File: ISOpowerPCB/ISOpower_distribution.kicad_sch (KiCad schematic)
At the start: 29 parts, among them M1 Fan_IEC60617, Q2 IRF5305_PBF, Q3 IRF5305_PBF, U10 LM2596S-5, U4 i6A4W020A-DC-DC-250W, U5 i6A4W020A-DC-DC-250W, U6 ACS712xLCTR-30A, U7 ACS712xLCTR-30A

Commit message: Started Routing V1
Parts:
- removed Q2, Q3: IRF5305_PBF, Package_TO_SOT_SMD:TO-263-2, symbol 000_MOSFET_Immo:IRF5305_PBF
- added Q2, Q3: Si2319CDS, Package_TO_SOT_SMD:SOT-23, symbol Transistor_FET:Si2319CDS
- R6, R7: footprint Resistor_THT:R_Axial_DIN0309_L9.0mm_D3.2mm_P12.70mm_Horizontal -> Resistor_THT:R_Axial_DIN0207_L6.3mm_D2.5mm_P7.62mm_Horizontal
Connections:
- net 12V_I_SENSE_OP is gone; now on net +12V: N2.1 (A), U7.3 (IP-), U7.4 (IP-)
- net 5V_I_SENSE_OP is gone; now on net +5V: N1.1 (A), U6.3 (IP-), U6.4 (IP-)
- net BUS_A_DISABLE: now also Q3.1 (G)
- net BUS_B_DISABLE: now also Q2.1 (G)
- net GND: now also Q2.3 (D), Q3.3 (D)
- net at JP2.2 (B), U4.2 (On/Off): now also Q2.2 (S)
- net at JP3.2 (B), U5.2 (On/Off): now also Q3.2 (S)
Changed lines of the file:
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@@
   (junction (at 246.38 133.35) (diameter 0) (color 0 0 0 0)
   )
+  (junction (at 173.99 64.77) (diameter 0) (color 0 0 0 0)
+  )
   (junction (at 205.74 128.27) (diameter 0) (color 0 0 0 0)
   )
@@
   (junction (at 246.38 143.51) (diameter 0) (color 0 0 0 0)
   )
+  (junction (at 179.07 64.77) (diameter 0) (color 0 0 0 0)
+  )
   (junction (at 39.37 39.37) (diameter 0) (color 0 0 0 0)
   )
@@
   (junction (at 113.03 64.77) (diameter 0) (color 0 0 0 0)
   )
+  (junction (at 170.18 143.51) (diameter 0) (color 0 0 0 0)
+  )
   (junction (at 121.92 143.51) (diameter 0) (color 0 0 0 0)
   )
@@
   )
   (junction (at 53.34 87.63) (diameter 0) (color 0 0 0 0)
+  )
+  (junction (at 175.26 143.51) (diameter 0) (color 0 0 0 0)
   )
   (junction (at 229.87 143.51) (diameter 0) (color 0 0 0 0)
@@
     (stroke (width 0) (type default) (color 0 0 0 0))
   )
-  (wire (pts (xy 149.86 143.51) (xy 171.45 143.51))
+  (wire (pts (xy 149.86 143.51) (xy 170.18 143.51))
     (stroke (width 0) (type default) (color 0 0 0 0))
   )
@@
     (stroke (width 0) (type default) (color 0 0 0 0))
   )
-  (wire (pts (xy 153.67 64.77) (xy 175.26 64.77))
+  (wire (pts (xy 153.67 64.77) (xy 173.99 64.77))
     (stroke (width 0) (type default) (color 0 0 0 0))
   )
@@
     (stroke (width 0) (type default) (color 0 0 0 0))
   )
-  (wire (pts (xy 176.53 143.51) (xy 173.99 143.51))
+  (wire (pts (xy 176.53 143.51) (xy 175.26 143.51))
     (stroke (width 0) (type default) (color 0 0 0 0))
   )
@@
     (stroke (width 0) (type default) (color 0 0 0 0))
   )
+  (wire (pts (xy 170.18 143.51) (xy 171.45 143.51))
+    (stroke (width 0) (type default) (color 0 0 0 0))
+  )
   (wire (pts (xy 59.69 153.67) (xy 59.69 154.94))
     (stroke (width 0) (type default) (color 0 0 0 0))
@@
     (stroke (width 0) (type default) (color 0 0 0 0))
   )
+  (wire (pts (xy 173.99 64.77) (xy 173.99 63.5))
+    (stroke (width 0) (type default) (color 0 0 0 0))
+  )
   (polyline (pts (xy 64.77 181.61) (xy 86.36 181.61))
     (stroke (width 0) (type default) (color 0 0 0 0))
   )
+  (wire (pts (xy 170.18 143.51) (xy 170.18 142.24))
+    (stroke (width 0) (type default) (color 0 0 0 0))
+  )
   (wire (pts (xy 246.38 143.51) (xy 246.38 142.24))
     (stroke (width 0) (type default) (color 0 0 0 0))
@@
     (stroke (width 0) (type default) (color 0 0 0 0))
   )
+  (wire (pts (xy 175.26 142.24) (xy 175.26 143.51))
+    (stroke (width 0) (type default) (color 0 0 0 0))
+  )
   (wire (pts (xy 246.38 134.62) (xy 246.38 133.35))
     (stroke (width 0) (type default) (color 0 0 0 0))
@@
     (stroke (width 0) (type default) (color 0 0 0 0))
   )
+  (wire (pts (xy 173.99 63.5) (xy 179.07 63.5))
+    (stroke (width 0) (type default) (color 0 0 0 0))
+  )
   (wire (pts (xy 41.91 80.01) (xy 41.91 81.28))
     (stroke (width 0) (type default) (color 0 0 0 0))
@@
     (stroke (width 0) (type default) (color 0 0 0 0))
   )
+  (wire (pts (xy 179.07 63.5) (xy 179.07 64.77))
+    (stroke (width 0) (type default) (color 0 0 0 0))
+  )
   (wire (pts (xy 143.51 64.77) (xy 143.51 62.23))
     (stroke (width 0) (type default) (color 0 0 0 0))
@@
     (stroke (width 0) (type default) (color 0 0 0 0))
   )
+  (wire (pts (xy 170.18 142.24) (xy 175.26 142.24))
+    (stroke (width 0) (type default) (color 0 0 0 0))
+  )
   (wire (pts (xy 41.91 146.05) (xy 41.91 143.51))
     (stroke (width 0) (type default) (color 0 0 0 0))
@@
     (stroke (width 0) (type default) (color 0 0 0 0))
   )
+  (wire (pts (xy 173.99 64.77) (xy 175.26 64.77))
+    (stroke (width 0) (type default) (color 0 0 0 0))
+  )
+  (wire (pts (xy 175.26 143.51) (xy 173.99 143.51))
+    (stroke (width 0) (type default) (color 0 0 0 0))
+  )
   (wire (pts (xy 217.17 133.35) (xy 214.63 133.35))
     (stroke (width 0) (type default) (color 0 0 0 0))
@@
     (stroke (width 0) (type default) (color 0 0 0 0))
   )
+  (wire (pts (xy 179.07 64.77) (xy 177.8 64.77))
+    (stroke (width 0) (type default) (color 0 0 0 0))
+  )
   (wire (pts (xy 158.75 125.73) (xy 158.75 130.81))
     (stroke (width 0) (type default) (color 0 0 0 0))
@@
     (stroke (width 0) (type default) (color 0 0 0 0))
   )
-  (wire (pts (xy 180.34 64.77) (xy 177.8 64.77))
+  (wire (pts (xy 180.34 64.77) (xy 179.07 64.77))
     (stroke (width 0) (type default) (color 0 0 0 0))
   )
@@
     (pin "2")
   )
+  (symbol (lib_id "Transistor_FET:Si2319CDS") (at 57.15 160.02 0) (mirror x) (unit 1)
+    (in_bom yes) (on_board yes)
+    (property "Reference" "Q2" (id 0) (at 60.96 154.94 90)
+      (effects (font (size 1.27 1.27)) (justify left))
+    )
+    (property "Value" "Si2319CDS" (id 1) (at 63.5 154.94 90)
+      (effects (font (size 1.27 1.27)) (justify left))
+    )
+    (property "Footprint" "Package_TO_SOT_SMD:SOT-23" (id 2) (at 62.23 158.115 0)
+      (effects (font (size 1.27 1.27) italic) (justify left) hide)
+    )
+    (property "Datasheet" "http://www.vishay.com/docs/66709/si2319cd.pdf" (id 3) (at 57.15 160.02 0)
+      (effects (font (size 1.27 1.27)) (justify left) hide)
+    )
+    (pin "1")
+    (pin "2")
+    (pin "3")
+  )
   (symbol (lib_id "000_Capacitor_Electrolytic_Immo:100u") (at 259.08 138.43 0) (unit 1)
     (in_bom yes) (on_board yes)
@@
       (effects (font (size 1.27 1.27)) (justify left))
     )
-    (property "Footprint" "Resistor_THT:R_Axial_DIN0309_L9.0mm_D3.2mm_P12.70mm_Horizontal" (id 2) (at 93.472 82.55 90)
+    (property "Footprint" "Resistor_THT:R_Axial_DIN0207_L6.3mm_D2.5mm_P7.62mm_Horizontal" (id 2) (at 93.472 82.55 90)
       (effects (font (size 1.27 1.27)) hide)
     )
@@
     (pin "1")
   )
-  (symbol (lib_id "000_MOSFET_Immo:IRF5305_PBF") (at 59.69 81.28 0) (mirror x) (unit 1)
-    (in_bom yes) (on_board yes)
-    (property "Reference" "Q3" (id 0) (at 57.15 83.82 90))
-    (property "Value" "IRF5305_PBF" (id 1) (at 66.04 81.28 90))
-    (property "Footprint" "Package_TO_SOT_SMD:TO-263-2" (id 2) (at 78.74 91.44 0)
+  (symbol (lib_id "Transistor_FET:Si2319CDS") (at 59.69 81.28 0) (mirror x) (unit 1)
+    (in_bom yes) (on_board yes)
+    (property "Reference" "Q3" (id 0) (at 63.5 76.2 90)
+      (effects (font (size 1.27 1.27)) (justify left))
+    )
+    (property "Value" "Si2319CDS" (id 1) (at 66.04 76.2 90)
+      (effects (font (size 1.27 1.27)) (justify left))
+    )
+    (property "Footprint" "Package_TO_SOT_SMD:SOT-23" (id 2) (at 64.77 79.375 0)
       (effects (font (size 1.27 1.27) italic) (justify left) hide)
     )
-    (property "Datasheet" "http://www.infineon.com/dgdl/irf4905.pdf?fileId=5546d462533600a4015355e32165197c" (id 3) (at 76.2 90.17 0)
-      (effects (font (size 1.27 1.27)) (justify left) hide)
-    )
-    (pin "1")
-    (pin "2")
-    (pin "3")
-  )
-  (symbol (lib_id "000_MOSFET_Immo:IRF5305_PBF") (at 57.15 160.02 0) (mirror x) (unit 1)
-    (in_bom yes) (on_board yes)
-    (property "Reference" "Q2" (id 0) (at 54.61 162.56 90))
-    (property "Value" "IRF5305_PBF" (id 1) (at 63.5 160.02 90))
-    (property "Footprint" "Package_TO_SOT_SMD:TO-263-2" (id 2) (at 76.2 170.18 0)
-      (effects (font (size 1.27 1.27) italic) (justify left) hide)
-    )
-    (property "Datasheet" "http://www.infineon.com/dgdl/irf4905.pdf?fileId=5546d462533600a4015355e32165197c" (id 3) (at 73.66 168.91 0)
+    (property "Datasheet" "http://www.vishay.com/docs/66709/si2319cd.pdf" (id 3) (at 59.69 81.28 0)
       (effects (font (size 1.27 1.27)) (justify left) hide)
     )
@@
       (effects (font (size 1.27 1.27)) (justify left))
     )
-    (property "Footprint" "Resistor_THT:R_Axial_DIN0309_L9.0mm_D3.2mm_P12.70mm_Horizontal" (id 2) (at 89.662 161.29 90)
-      (effects (font (size 1.27 1.27)) hide)
-    )
+    (property "Footprint" "Resistor_THT:R_Axial_DIN0207_L6.3mm_D2.5mm_P7.62mm_Horizontal" (id 2) (at 89.662 161.29 90)
+      (effects (font (size 1.27 1.27)) hide)
+    )

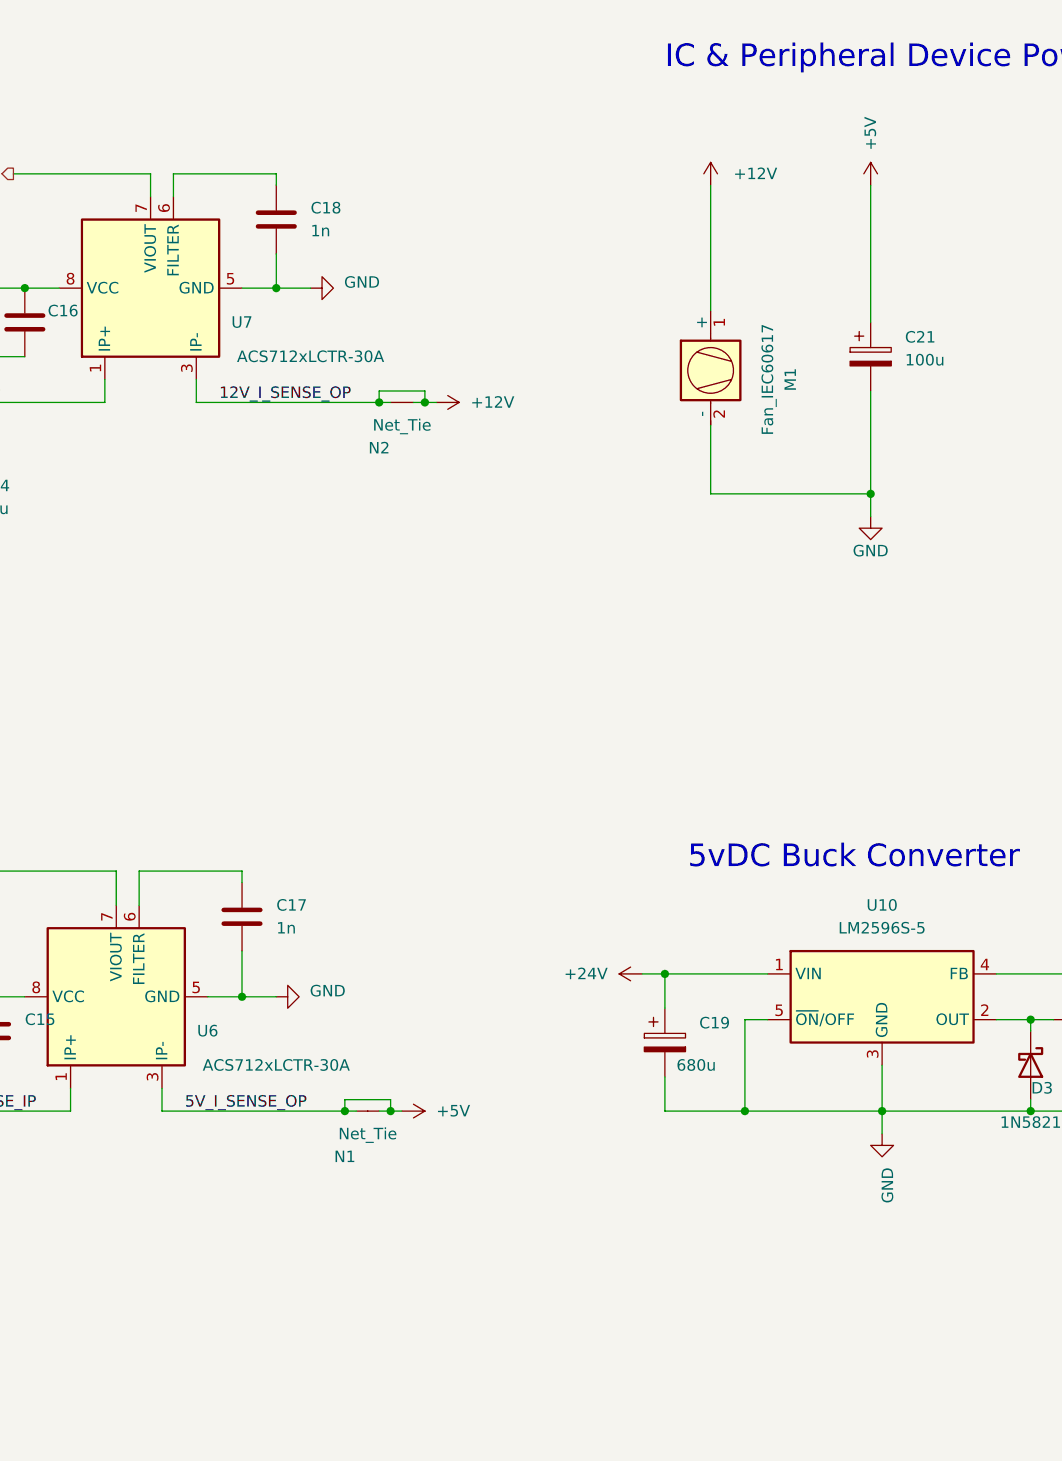
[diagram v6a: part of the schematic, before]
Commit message: Replacing power bus RE current draw issue
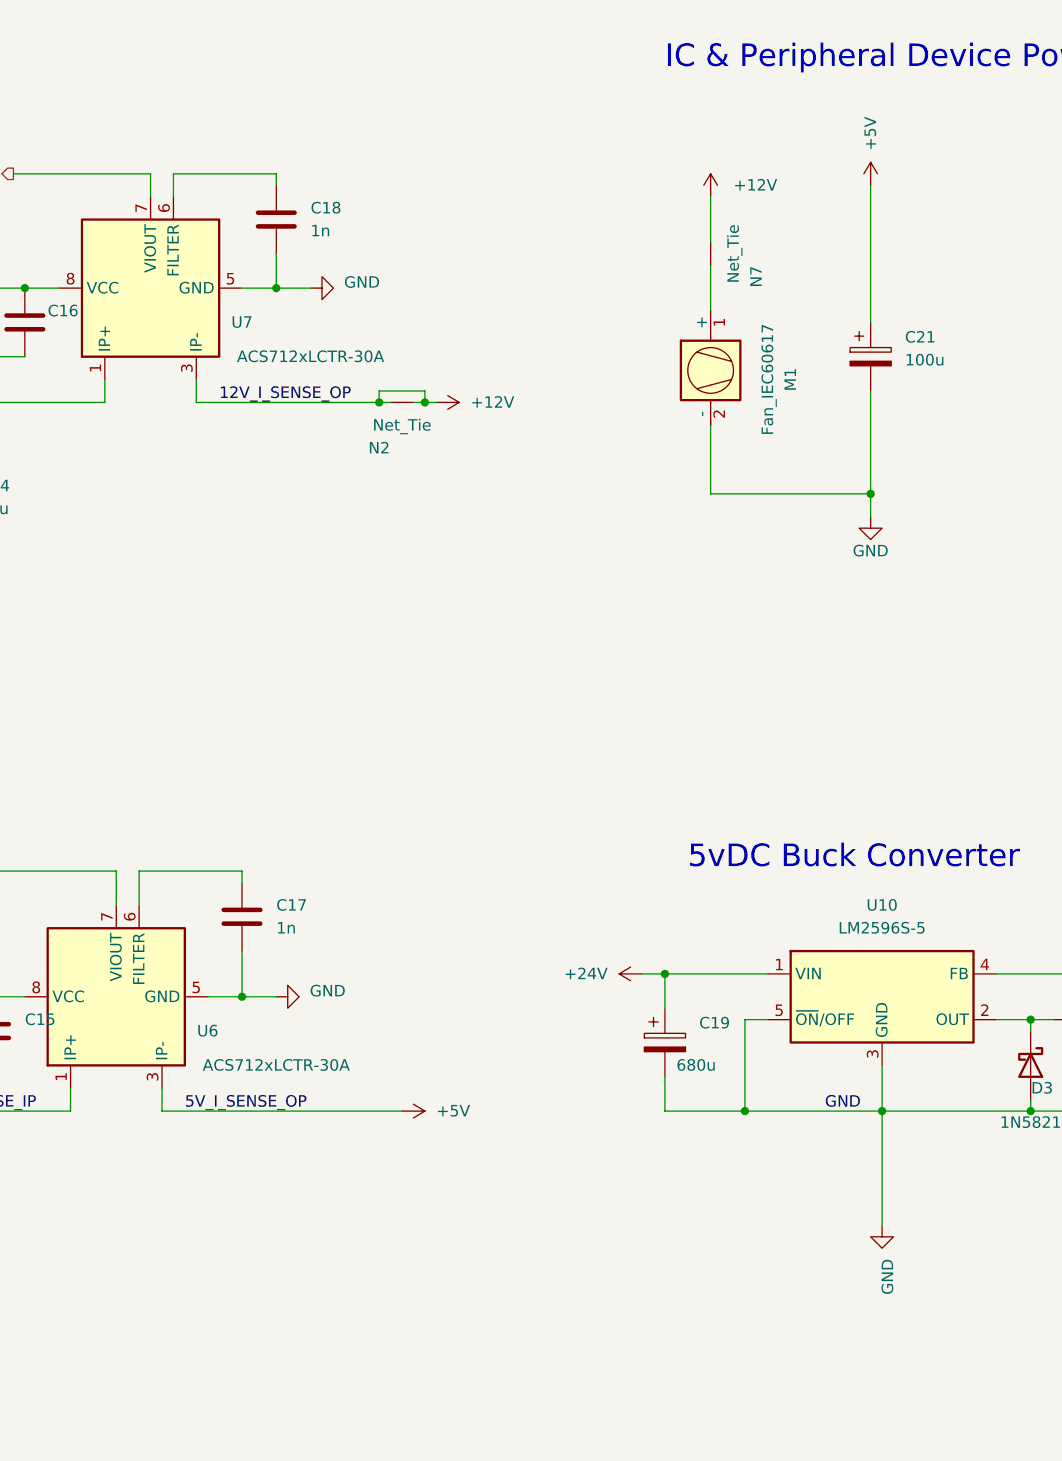
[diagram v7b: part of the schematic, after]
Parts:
- removed N1: Net_Tie, NetTie:NetTie-2_SMD_Pad0.5mm, symbol 000_Utility_Immo:Net_Tie
- added N7: Net_Tie, NetTie:NetTie-2_SMD_Pad0.5mm, symbol 000_Utility_Immo:Net_Tie
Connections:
- net +12V: now also N7.2 (C); no longer M1.1 (+)
- new net: M1.1 (+), N7.1 (A)
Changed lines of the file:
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@@
   (junction (at 113.03 64.77) (diameter 0) (color 0 0 0 0)
   )
-  (junction (at 170.18 143.51) (diameter 0) (color 0 0 0 0)
-  )
   (junction (at 121.92 143.51) (diameter 0) (color 0 0 0 0)
   )
@@
   )
   (junction (at 53.34 87.63) (diameter 0) (color 0 0 0 0)
-  )
-  (junction (at 175.26 143.51) (diameter 0) (color 0 0 0 0)
   )
   (junction (at 229.87 143.51) (diameter 0) (color 0 0 0 0)
@@
     (stroke (width 0) (type default) (color 0 0 0 0))
   )
-  (wire (pts (xy 149.86 143.51) (xy 170.18 143.51))
+  (wire (pts (xy 149.86 143.51) (xy 176.53 143.51))
     (stroke (width 0) (type default) (color 0 0 0 0))
   )
@@
     (stroke (width 0) (type default) (color 0 0 0 0))
   )
+  (wire (pts (xy 229.87 143.51) (xy 229.87 156.21))
+    (stroke (width 0) (type default) (color 0 0 0 0))
+  )
   (wire (pts (xy 228.6 63.5) (xy 228.6 74.93))
     (stroke (width 0) (type default) (color 0 0 0 0))
@@
     (stroke (width 0) (type default) (color 0 0 0 0))
   )
-  (wire (pts (xy 176.53 143.51) (xy 175.26 143.51))
-    (stroke (width 0) (type default) (color 0 0 0 0))
-  )
   (wire (pts (xy 59.69 165.1) (xy 59.69 166.37))
     (stroke (width 0) (type default) (color 0 0 0 0))
@@
     (stroke (width 0) (type default) (color 0 0 0 0))
   )
-  (wire (pts (xy 170.18 143.51) (xy 171.45 143.51))
-    (stroke (width 0) (type default) (color 0 0 0 0))
-  )
   (wire (pts (xy 59.69 153.67) (xy 59.69 154.94))
     (stroke (width 0) (type default) (color 0 0 0 0))
@@
     (stroke (width 0) (type default) (color 0 0 0 0))
   )
-  (wire (pts (xy 210.82 40.64) (xy 210.82 54.61))
-    (stroke (width 0) (type default) (color 0 0 0 0))
-  )
   (wire (pts (xy 41.91 153.67) (xy 41.91 166.37))
     (stroke (width 0) (type default) (color 0 0 0 0))
@@
     (stroke (width 0) (type default) (color 0 0 0 0))
   )
-  (wire (pts (xy 170.18 143.51) (xy 170.18 142.24))
-    (stroke (width 0) (type default) (color 0 0 0 0))
-  )
   (wire (pts (xy 246.38 143.51) (xy 246.38 142.24))
     (stroke (width 0) (type default) (color 0 0 0 0))
@@
     (stroke (width 0) (type default) (color 0 0 0 0))
   )
+  (wire (pts (xy 210.82 49.53) (xy 210.82 54.61))
+    (stroke (width 0) (type default) (color 0 0 0 0))
+  )
   (wire (pts (xy 95.25 64.77) (xy 113.03 64.77))
     (stroke (width 0) (type default) (color 0 0 0 0))
@@
     (stroke (width 0) (type default) (color 0 0 0 0))
   )
-  (wire (pts (xy 175.26 142.24) (xy 175.26 143.51))
-    (stroke (width 0) (type default) (color 0 0 0 0))
-  )
   (wire (pts (xy 246.38 134.62) (xy 246.38 133.35))
     (stroke (width 0) (type default) (color 0 0 0 0))
@@
     (stroke (width 0) (type default) (color 0 0 0 0))
   )
-  (wire (pts (xy 229.87 143.51) (xy 229.87 146.05))
-    (stroke (width 0) (type default) (color 0 0 0 0))
-  )
   (wire (pts (xy 229.87 143.51) (xy 246.38 143.51))
     (stroke (width 0) (type default) (color 0 0 0 0))
@@
     (stroke (width 0) (type default) (color 0 0 0 0))
   )
-  (wire (pts (xy 170.18 142.24) (xy 175.26 142.24))
-    (stroke (width 0) (type default) (color 0 0 0 0))
-  )
   (wire (pts (xy 41.91 146.05) (xy 41.91 143.51))
     (stroke (width 0) (type default) (color 0 0 0 0))
@@
     (stroke (width 0) (type default) (color 0 0 0 0))
   )
-  (wire (pts (xy 175.26 143.51) (xy 173.99 143.51))
-    (stroke (width 0) (type default) (color 0 0 0 0))
-  )
   (wire (pts (xy 217.17 133.35) (xy 214.63 133.35))
     (stroke (width 0) (type default) (color 0 0 0 0))
@@
   )
   (wire (pts (xy 127 52.07) (xy 134.62 52.07))
+    (stroke (width 0) (type default) (color 0 0 0 0))
+  )
+  (wire (pts (xy 210.82 41.91) (xy 210.82 46.99))
     (stroke (width 0) (type default) (color 0 0 0 0))
   )
@@
   )
   (label "24V_BUS" (at 29.21 21.59 0)
+    (effects (font (size 1.27 1.27)) (justify left bottom))
+  )
+  (label "GND" (at 223.52 143.51 0)
     (effects (font (size 1.27 1.27)) (justify left bottom))
   )
@@
     (pin "2")
   )
-  (symbol (lib_id "power:GND") (at 229.87 146.05 0) (unit 1)
-    (in_bom yes) (on_board yes)
-    (property "Reference" "#PWR051" (id 0) (at 229.87 152.4 0)
-      (effects (font (size 1.27 1.27)) hide)
-    )
-    (property "Value" "GND" (id 1) (at 230.505 151.765 90))
-    (property "Footprint" "" (id 2) (at 229.87 146.05 0)
-      (effects (font (size 1.27 1.27)) hide)
-    )
-    (property "Datasheet" "" (id 3) (at 229.87 146.05 0)
+  (symbol (lib_id "power:GND") (at 229.87 156.21 0) (unit 1)
+    (in_bom yes) (on_board yes)
+    (property "Reference" "#PWR051" (id 0) (at 229.87 162.56 0)
+      (effects (font (size 1.27 1.27)) hide)
+    )
+    (property "Value" "GND" (id 1) (at 230.505 161.925 90))
+    (property "Footprint" "" (id 2) (at 229.87 156.21 0)
+      (effects (font (size 1.27 1.27)) hide)
+    )
+    (property "Datasheet" "" (id 3) (at 229.87 156.21 0)
       (effects (font (size 1.27 1.27)) hide)
     )
@@
     )
     (pin "1")
+  )
+  (symbol (lib_id "000_Utility_Immo:Net_Tie") (at 210.82 48.26 90) (unit 1)
+    (in_bom no) (on_board yes)
+    (property "Reference" "N7" (id 0) (at 215.9 50.8 0))
+    (property "Value" "Net_Tie" (id 1) (at 213.36 48.26 0))
+    (property "Footprint" "NetTie:NetTie-2_SMD_Pad0.5mm" (id 2) (at 213.36 48.26 0)
+      (effects (font (size 1.27 1.27)) hide)
+    )
+    (property "Datasheet" "~" (id 3) (at 209.55 48.26 0)
+      (effects (font (size 1.27 1.27)) hide)
+    )
+    (pin "1")
+    (pin "2")
   )
   (symbol (lib_id "000_Capacitor_Film_Immo:cap_film_0805") (at 158.75 121.92 0) (unit 1)
@@
     (pin "1")
   )
-  (symbol (lib_id "power:+12V") (at 210.82 40.64 0) (unit 1)
-    (in_bom yes) (on_board yes) (fields_autoplaced)
-    (property "Reference" "#PWR047" (id 0) (at 210.82 44.45 0)
-      (effects (font (size 1.27 1.27)) hide)
-    )
-    (property "Value" "+12V" (id 1) (at 213.36 39.3699 0)
-      (effects (font (size 1.27 1.27)) (justify left))
-    )
-    (property "Footprint" "" (id 2) (at 210.82 40.64 0)
-      (effects (font (size 1.27 1.27)) hide)
-    )
-    (property "Datasheet" "" (id 3) (at 210.82 40.64 0)
+  (symbol (lib_id "power:+12V") (at 210.82 41.91 0) (unit 1)
+    (in_bom yes) (on_board yes) (fields_autoplaced)
+    (property "Reference" "#PWR047" (id 0) (at 210.82 45.72 0)
+      (effects (font (size 1.27 1.27)) hide)
+    )
+    (property "Value" "+12V" (id 1) (at 213.36 40.6399 0)
+      (effects (font (size 1.27 1.27)) (justify left))
+    )
+    (property "Footprint" "" (id 2) (at 210.82 41.91 0)
+      (effects (font (size 1.27 1.27)) hide)
+    )
+    (property "Datasheet" "" (id 3) (at 210.82 41.91 0)
       (effects (font (size 1.27 1.27)) hide)
     )
@@
     (pin "1")
   )
-  (symbol (lib_id "000_Utility_Immo:Net_Tie") (at 172.72 143.51 0) (unit 1)
-    (in_bom no) (on_board yes)
-    (property "Reference" "N1" (id 0) (at 170.18 148.59 0))
-    (property "Value" "Net_Tie" (id 1) (at 172.72 146.05 0))
-    (property "Footprint" "NetTie:NetTie-2_SMD_Pad0.5mm" (id 2) (at 172.72 146.05 0)
-      (effects (font (size 1.27 1.27)) hide)
-    )
-    (property "Datasheet" "~" (id 3) (at 172.72 142.24 0)
-      (effects (font (size 1.27 1.27)) hide)
-    )
-    (pin "1")
-    (pin "2")
-  )
 )
